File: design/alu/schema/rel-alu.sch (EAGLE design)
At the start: 33 parts, among them IC1 74LS04N, IC2 74LS04N, IC3 74LS04N, IC35 74LS32N, IC37 74LS08N, IC38 74LS08N, IC39 74LS32N, IC4 74LS04N, IC41 74LS08N, IC42 74LS32N, IC44 74LS08N, IC45 74LS32N, IC46 74LS86N, IC47 74LS86N, IC48 74LS32N, IC5 74LS04N, IC50 74LS08N, IC51 74LS08N, IC52 74LS32N, IC54 74LS08N, IC55 74LS32N, IC57 74LS08N, IC58 74LS32N, IC59 74LS245N, IC6 74LS04N, IC7 74LS04N, IC8 74LS04N

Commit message: Added initial schema for general purpose registers
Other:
- moved on the sheet: DUAL-4X1-MUX-2, DUAL-4X1-MUX-3, IC46A, IC46B, IC46C, IC46D, IC47A, IC47B, IC47C, IC47D, IC48D, IC50D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

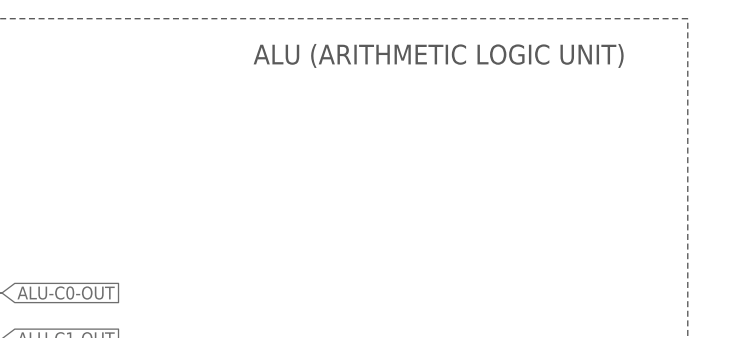
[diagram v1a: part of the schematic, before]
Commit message: Aligned titles size for all schemas
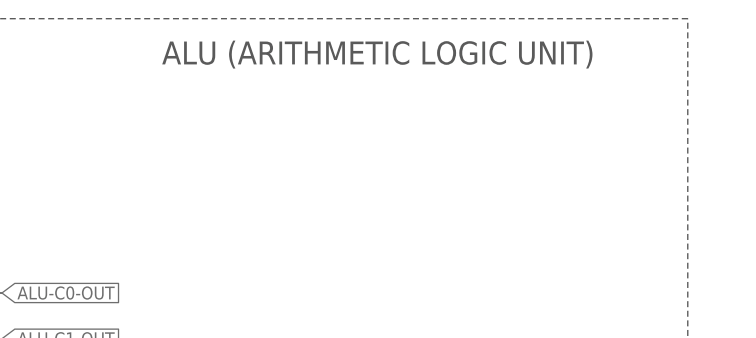
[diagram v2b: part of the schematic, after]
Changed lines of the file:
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@@
 <wire x1="78.74" y1="429.26" x2="-167.64" y2="429.26" width="0.1524" layer="97" style="shortdash"/>
 <wire x1="-167.64" y1="429.26" x2="-167.64" y2="421.64" width="0.1524" layer="97" style="shortdash"/>
-<text x="30.48" y="424.18" size="2.1844" layer="97">ALU (ARITHMETIC LOGIC UNIT)</text>
+<text x="20.32" y="424.18" size="2.54" layer="97">ALU (ARITHMETIC LOGIC UNIT)</text>
 </plain>
 <instances>

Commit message: Added version number to each schema
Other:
- note added: "VER 1.3"
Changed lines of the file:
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@@
 <?xml version="1.0" encoding="utf-8"?>
 <!DOCTYPE eagle SYSTEM "eagle.dtd">
-<eagle version="9.1.3">
+<eagle version="9.6.2">
 <drawing>
 <settings>
@@
 <wire x1="-167.64" y1="429.26" x2="-167.64" y2="421.64" width="0.1524" layer="97" style="shortdash"/>
 <text x="20.32" y="424.18" size="2.54" layer="97">ALU (ARITHMETIC LOGIC UNIT)</text>
+<wire x1="10.16" y1="22.86" x2="10.16" y2="7.62" width="0.1524" layer="97"/>
+<wire x1="10.16" y1="7.62" x2="73.66" y2="7.62" width="0.1524" layer="97"/>
+<wire x1="73.66" y1="7.62" x2="73.66" y2="22.86" width="0.1524" layer="97"/>
+<wire x1="73.66" y1="22.86" x2="10.16" y2="22.86" width="0.1524" layer="97"/>
+<text x="17.78" y="12.7" size="5.08" layer="97">VER 1.3</text>
 </plain>
 <instances>
@@
 <attribute name="VALUE" x="-55.88" y="40.64" size="1.778" layer="96"/>
 </instance>
-<instance part="IC59" gate="A" x="25.4" y="226.06"/>
+<instance part="IC59" gate="A" x="25.4" y="226.06" smashed="yes">
+<attribute name="NAME" x="17.78" y="241.935" size="1.778" layer="95"/>
+<attribute name="VALUE" x="17.78" y="208.28" size="1.778" layer="96"/>
+</instance>
 <instance part="SUPPLY1" gate="G$1" x="-7.62" y="251.46" smashed="yes">
 <attribute name="VALUE" x="-12.065" y="254.635" size="1.778" layer="96"/>
 </instance>
-<instance part="IC1" gate="A" x="-91.44" y="421.64"/>
-<instance part="IC2" gate="A" x="-91.44" y="381"/>
-<instance part="IC3" gate="A" x="-91.44" y="337.82"/>
-<instance part="IC4" gate="A" x="-91.44" y="297.18"/>
-<instance part="IC5" gate="A" x="-55.88" y="198.12"/>
-<instance part="IC6" gate="A" x="-55.88" y="157.48"/>
-<instance part="IC7" gate="A" x="-55.88" y="114.3"/>
-<instance part="IC8" gate="A" x="-55.88" y="73.66"/>
+<instance part="IC1" gate="A" x="-91.44" y="421.64" smashed="yes">
+<attribute name="NAME" x="-88.9" y="424.815" size="1.778" layer="95"/>
+<attribute name="VALUE" x="-88.9" y="416.56" size="1.778" layer="96"/>
+</instance>
+<instance part="IC2" gate="A" x="-91.44" y="381" smashed="yes">
+<attribute name="NAME" x="-88.9" y="384.175" size="1.778" layer="95"/>
+<attribute name="VALUE" x="-88.9" y="375.92" size="1.778" layer="96"/>
+</instance>
+<instance part="IC3" gate="A" x="-91.44" y="337.82" smashed="yes">
+<attribute name="NAME" x="-88.9" y="340.995" size="1.778" layer="95"/>
+<attribute name="VALUE" x="-88.9" y="332.74" size="1.778" layer="96"/>
+</instance>
+<instance part="IC4" gate="A" x="-91.44" y="297.18" smashed="yes">
+<attribute name="NAME" x="-88.9" y="300.355" size="1.778" layer="95"/>
+<attribute name="VALUE" x="-88.9" y="292.1" size="1.778" layer="96"/>
+</instance>
+<instance part="IC5" gate="A" x="-55.88" y="198.12" smashed="yes">
+<attribute name="NAME" x="-53.34" y="201.295" size="1.778" layer="95"/>
+<attribute name="VALUE" x="-53.34" y="193.04" size="1.778" layer="96"/>
+</instance>
+<instance part="IC6" gate="A" x="-55.88" y="157.48" smashed="yes">
+<attribute name="NAME" x="-53.34" y="160.655" size="1.778" layer="95"/>
+<attribute name="VALUE" x="-53.34" y="152.4" size="1.778" layer="96"/>
+</instance>
+<instance part="IC7" gate="A" x="-55.88" y="114.3" smashed="yes">
+<attribute name="NAME" x="-53.34" y="117.475" size="1.778" layer="95"/>
+<attribute name="VALUE" x="-53.34" y="109.22" size="1.778" layer="96"/>
+</instance>
+<instance part="IC8" gate="A" x="-55.88" y="73.66" smashed="yes">
+<attribute name="NAME" x="-53.34" y="76.835" size="1.778" layer="95"/>
+<attribute name="VALUE" x="-53.34" y="68.58" size="1.778" layer="96"/>
+</instance>
 <instance part="GND3" gate="1" x="-27.94" y="360.68" smashed="yes">
 <attribute name="VALUE" x="-30.48" y="358.14" size="1.778" layer="96"/>

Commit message: Fixed substraction arithmetic
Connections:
- removed net ADD0-A0-IN: 4BIT-FULL-ADDER-2A.A1, IC46A.O
- removed net ADD0-A1-IN: 4BIT-FULL-ADDER-2A.A2, IC46B.O
- removed net ADD0-A2-IN: 4BIT-FULL-ADDER-2A.A3, IC46C.O
- removed net ADD0-A3-IN: 4BIT-FULL-ADDER-2A.A4, IC46D.O
- removed net ADD1-A4-IN: 4BIT-FULL-ADDER-3A.A1, IC47A.O
- removed net ADD1-A5-IN: 4BIT-FULL-ADDER-3A.A2, IC47B.O
- removed net ADD1-A6-IN: 4BIT-FULL-ADDER-3A.A3, IC47C.O
- removed net ADD1-A7-IN: 4BIT-FULL-ADDER-3A.A4, IC47D.O
- new net ADD0-B0-IN: 4BIT-FULL-ADDER-2A.B1, IC46A.O
- new net ADD0-B1-IN: 4BIT-FULL-ADDER-2A.B2, IC46B.O
- new net ADD0-B2-IN: 4BIT-FULL-ADDER-2A.B3, IC46C.O
- new net ADD0-B3-IN: 4BIT-FULL-ADDER-2A.B4, IC46D.O
- new net ADD1-B4-IN: 4BIT-FULL-ADDER-3A.B1, IC47A.O
- new net ADD1-B5-IN: 4BIT-FULL-ADDER-3A.B2, IC47B.O
- new net ADD1-B6-IN: 4BIT-FULL-ADDER-3A.B3, IC47C.O
- new net ADD1-B7-IN: 4BIT-FULL-ADDER-3A.B4, IC47D.O
- net ALU-A0-IN: now also 4BIT-FULL-ADDER-2A.A1; no longer IC46A.I1
- net ALU-A1-IN: now also 4BIT-FULL-ADDER-2A.A2; no longer IC46B.I1
- net ALU-A2-IN: now also 4BIT-FULL-ADDER-2A.A3; no longer IC46C.I1
- net ALU-A3-IN: now also 4BIT-FULL-ADDER-2A.A4; no longer IC46D.I1
- net ALU-A4-IN: now also 4BIT-FULL-ADDER-3A.A1; no longer IC47A.I1
- net ALU-A5-IN: now also 4BIT-FULL-ADDER-3A.A2; no longer IC47B.I1
- net ALU-A6-IN: now also 4BIT-FULL-ADDER-3A.A3; no longer IC47C.I1
- net ALU-A7-IN: now also 4BIT-FULL-ADDER-3A.A4; no longer IC47D.I1
- net ALU-B0-IN: now also IC46A.I1; no longer 4BIT-FULL-ADDER-2A.B1
- net ALU-B1-IN: now also IC46B.I1; no longer 4BIT-FULL-ADDER-2A.B2
- net ALU-B2-IN: now also IC46C.I1; no longer 4BIT-FULL-ADDER-2A.B3
- net ALU-B3-IN: now also IC46D.I1; no longer 4BIT-FULL-ADDER-2A.B4
- net ALU-B4-IN: now also IC47A.I1; no longer 4BIT-FULL-ADDER-3A.B1
- net ALU-B5-IN: now also IC47B.I1; no longer 4BIT-FULL-ADDER-3A.B2
- net ALU-B6-IN: now also IC47C.I1; no longer 4BIT-FULL-ADDER-3A.B3
- net ALU-B7-IN: now also IC47D.I1; no longer 4BIT-FULL-ADDER-3A.B4
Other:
- note added: "VER 1.4"
- note removed: "VER 1.3"

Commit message: Added additional buffer to pull-up signals on diect connection to ALU
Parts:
- renumbered 4BIT-FULL-ADDER-2 to 4BIT-FULL-ADDER-0, 4BIT-FULL-ADDER-3 to 4BIT-FULL-ADDER-1, IC1 to INVERTER0-A0-, IC2 to INVERTER0-A1-, IC3 to INVERTER0-A2-, IC35 to OR-AB0-, IC37 to AND0-AB0-, IC38 to AND0-AB1-, IC39 to OR0-AB1-, IC4 to INVERTER0-A3-, IC41 to AND0-AB2-, IC42 to OR0-AB2-, IC44 to AND0-AB3-, IC45 to OR0-AB3-, IC46 to XOR0-B, IC47 to XOR1-B, IC48 to OR1-AB4-, IC5 to INVERTER1-A4-, IC50 to AND1-AB4-, IC51 to AND1-AB5-, IC52 to OR1-AB5-, IC54 to AND1-AB6-, IC55 to OR1-AB6-, IC57 to AND1-AB7-, IC58 to OR1-AB7-, IC59 to BUFFER-OUT, IC6 to INVERTER1-A5-, IC7 to INVERTER1-A6-, IC8 to INVERTER1-A7-
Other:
- note added: "VER 1.5"
- note removed: "VER 1.4"
